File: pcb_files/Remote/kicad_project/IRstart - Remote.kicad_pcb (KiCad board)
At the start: 2 copper layers, 40 x 59.4 mm, 50 parts, among them SW1 SW_DIP_x02, SW2 SW_DIP_x02, SW3 SW_DPDT_x2

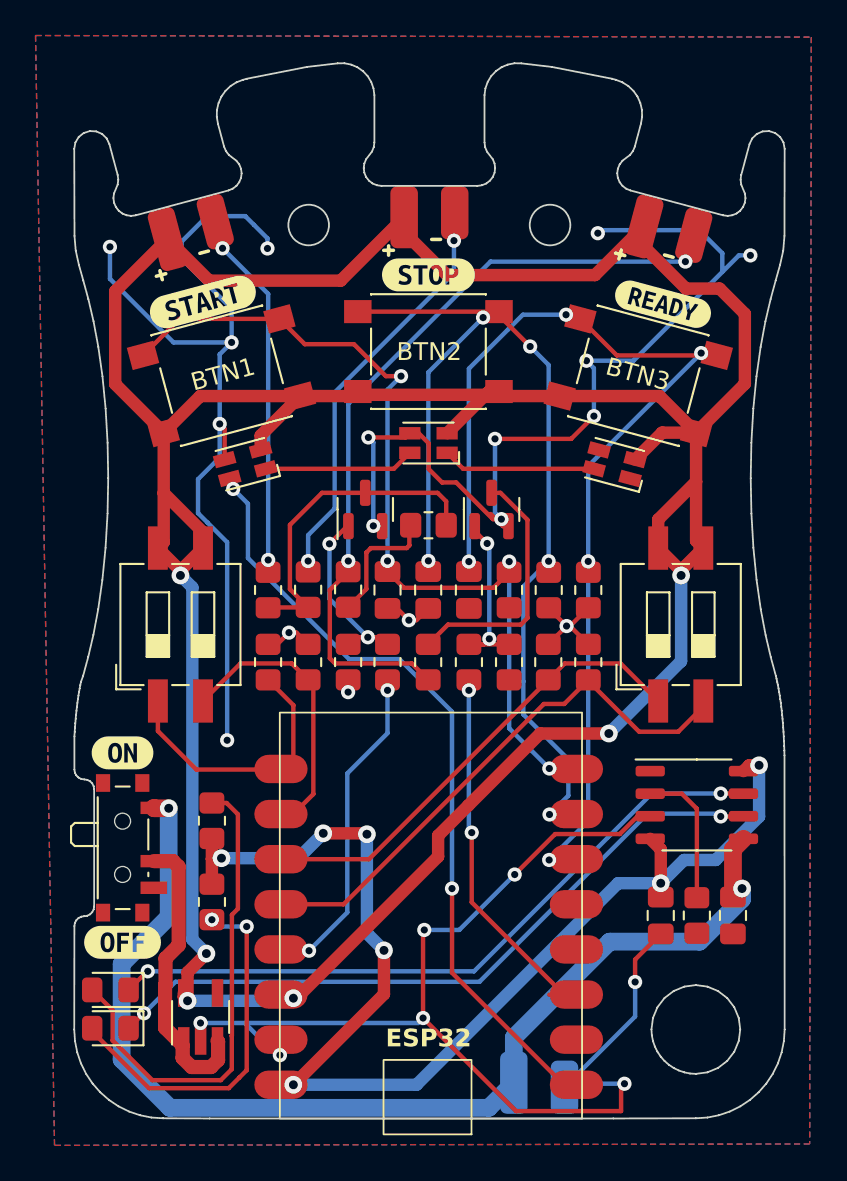
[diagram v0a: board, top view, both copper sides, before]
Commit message: Añade gerbers de remote y adecenta el esquematico
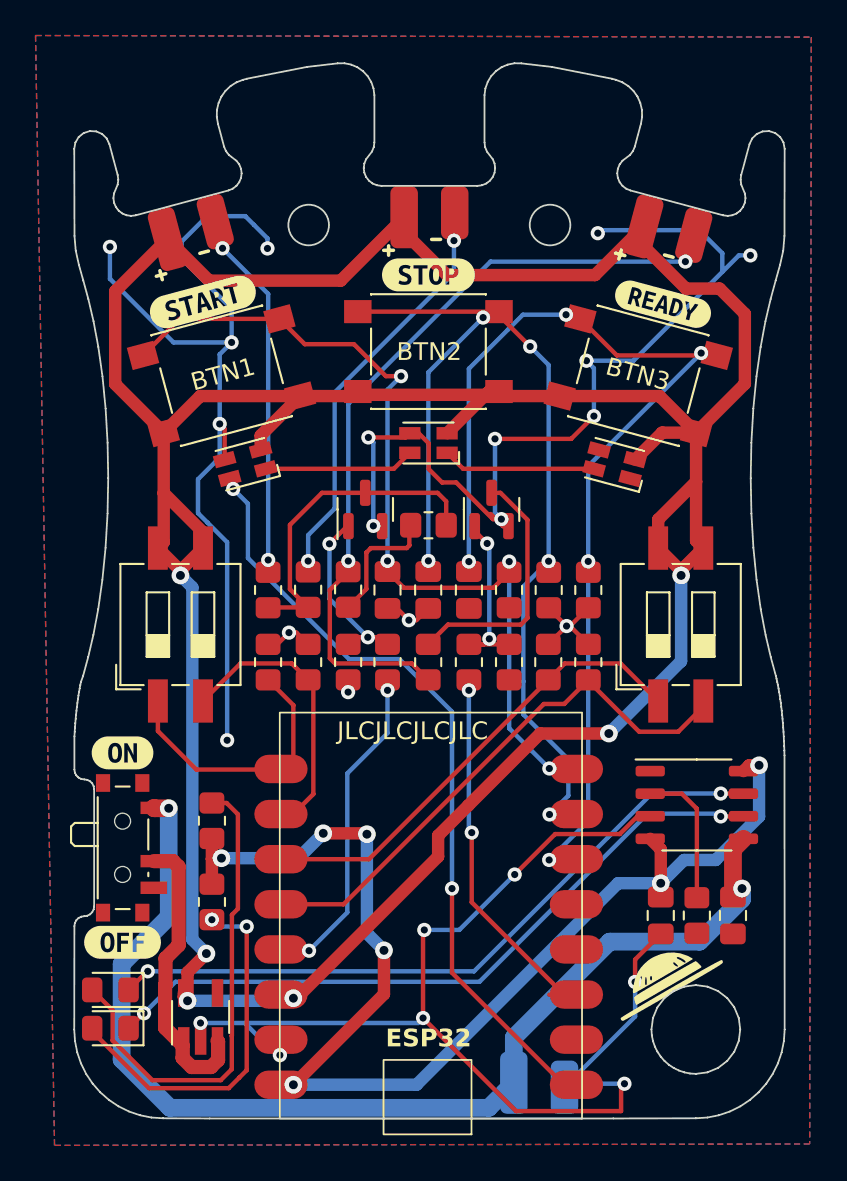
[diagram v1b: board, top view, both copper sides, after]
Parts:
- added G***: LOGO, LOGO, F.Cu at (167.2, 120.6)
- added G***: LOGO, LOGO, B.Cu at (138.6, 122.9)
- added kibuzzard-664F31E4: G***, kibuzzard-664F31E4, B.Cu at (153.7, 81.2)
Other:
- board text added: "JLCJLCJLCJLC"
